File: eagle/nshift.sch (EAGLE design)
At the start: 15 parts, among them IC1 TINY13V-10PU, IC2 7805T, Q1 IRF510, Q2 IRF510

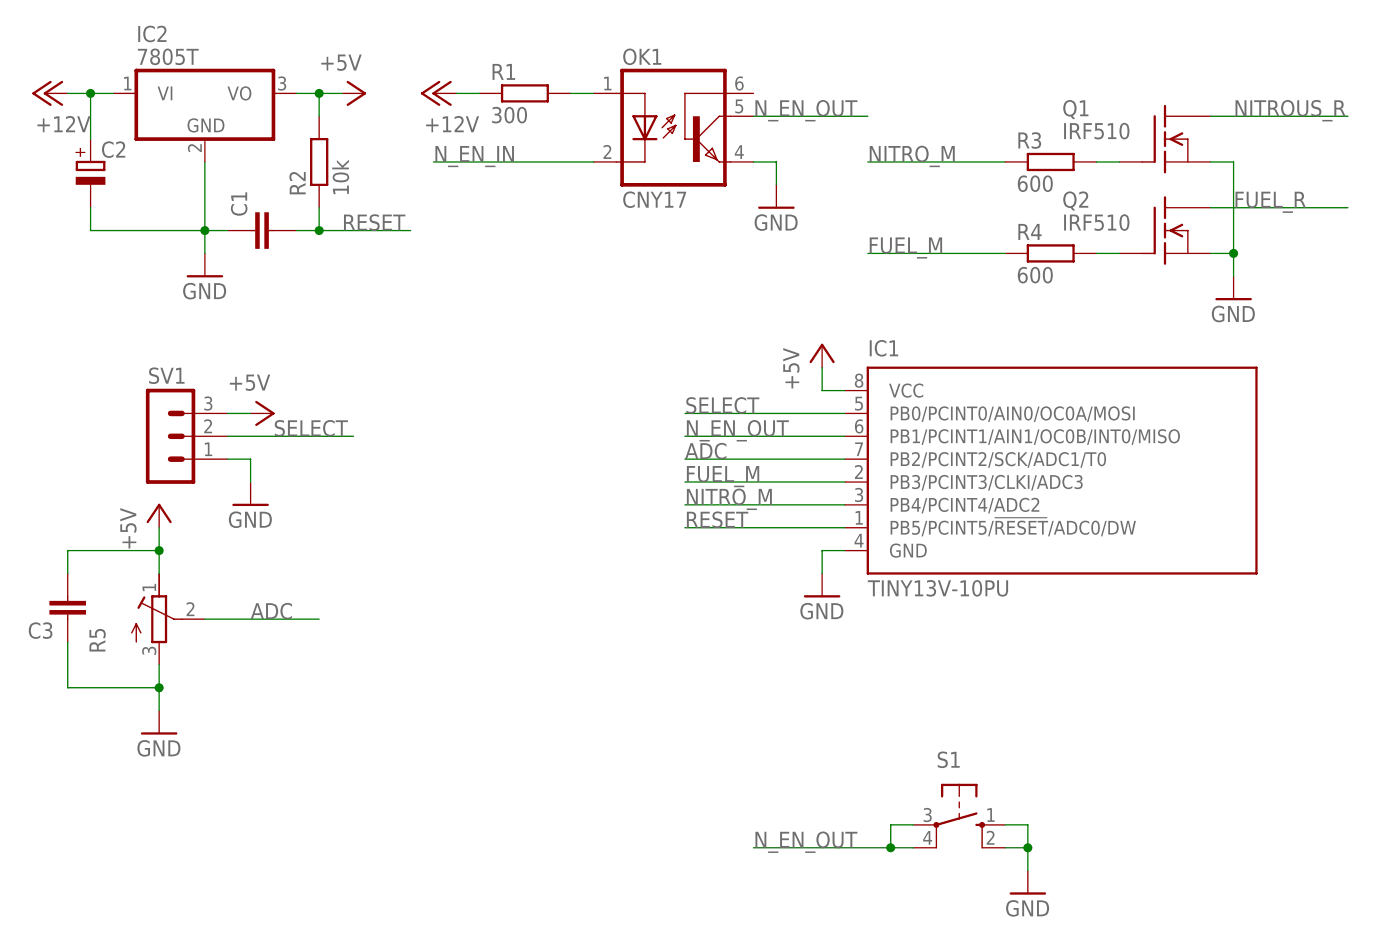
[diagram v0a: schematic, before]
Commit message: refactor for new soic components
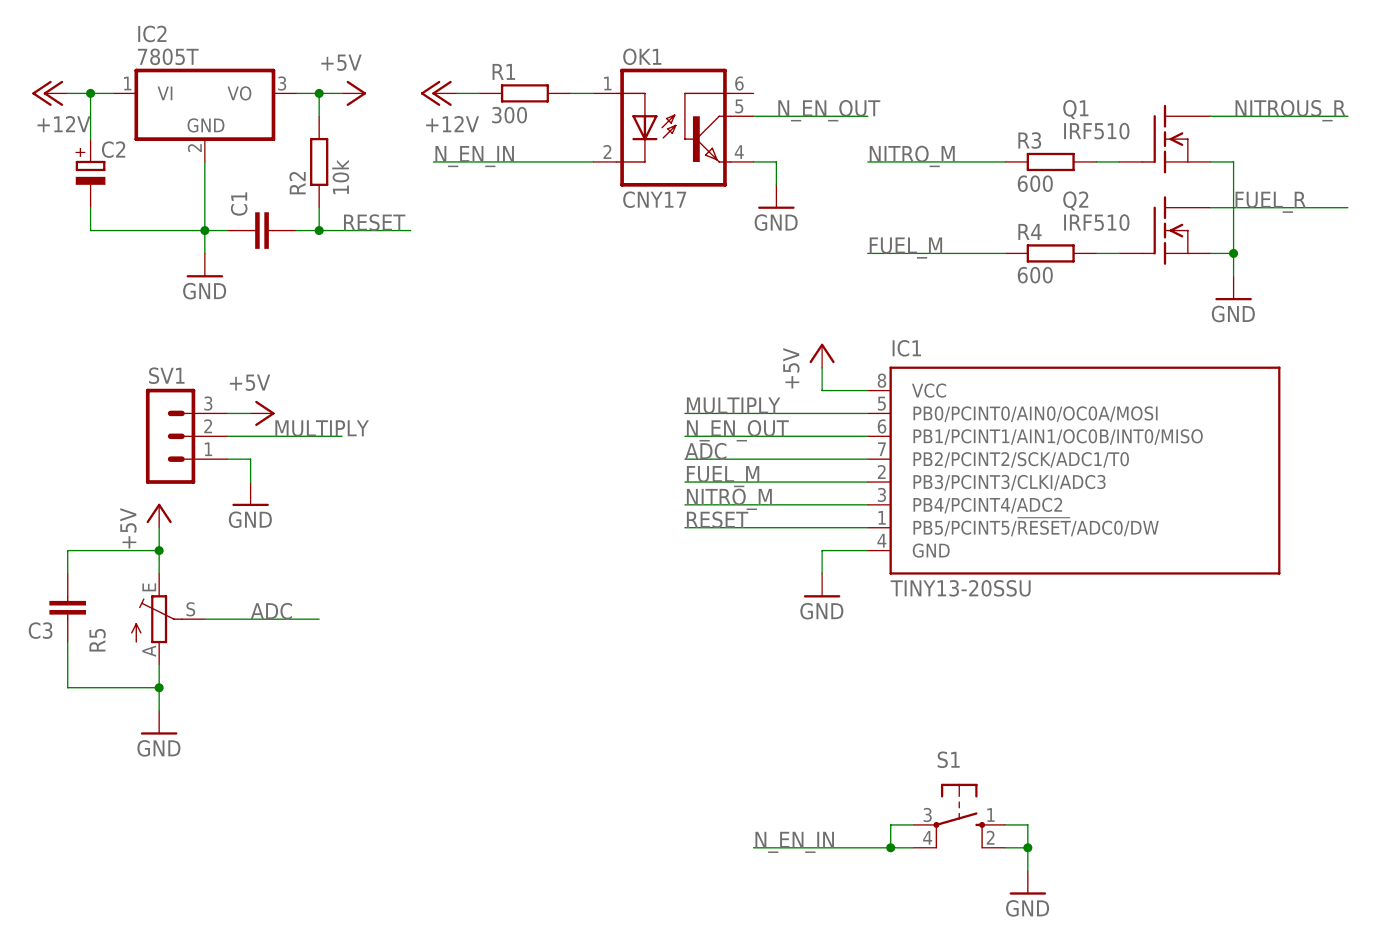
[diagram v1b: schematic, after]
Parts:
- IC1: value TINY13V-10PU -> TINY13-20SSU; device atmel:TINY13V-10PU -> atmel:TINY13-20SSU
- R5: device resistor:R-TRIMMT93XB -> pot:TRIM_EU-CA9V
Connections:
- net SELECT renamed MULTIPLY
- net +5V: now also R5.E; no longer R5.A
- net GND: now also R5.A; no longer R5.E
- net N_EN_IN: now also S1.P, S1.P1
- net N_EN_OUT: no longer S1.P, S1.P1
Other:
- moved on the sheet: IC1
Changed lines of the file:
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@@
 <setting verticaltext="up"/>
 </settings>
-<grid distance="0.05" unitdist="inch" unit="inch" style="dots" multiple="1" display="yes" altdistance="0.01" altunitdist="inch" altunit="inch"/>
+<grid distance="0.1" unitdist="inch" unit="inch" style="lines" multiple="1" display="no" altdistance="0.01" altunitdist="inch" altunit="inch"/>
 <layers>
 <layer number="1" name="Top" color="4" fill="1" visible="no" active="no"/>
@@
 </classes>
 <parts>
-<part name="IC1" library="atmel" deviceset="TINY13" device="PU" technology="V-10"/>
+<part name="IC1" library="atmel" library_urn="urn:adsk.eagle:library:105" deviceset="TINY13" device="SSU" technology="-20" value="TINY13-20SSU"/>
 <part name="OK1" library="optocoupler" deviceset="CNY17" device=""/>
 <part name="Q1" library="transistor-fet" deviceset="IRF510" device=""/>
@@
 <part name="R3" library="resistor" deviceset="R-EU_" device="0207/7" value="600"/>
 <part name="R4" library="resistor" deviceset="R-EU_" device="0207/7" value="600"/>
-<part name="R5" library="resistor" deviceset="R-TRIMM" device="T93XB"/>
+<part name="R5" library="pot" library_urn="urn:adsk.eagle:library:331" deviceset="TRIM_EU-" device="CA9V"/>
 <part name="P+6" library="supply1" deviceset="+5V" device=""/>
 <part name="GND6" library="supply1" deviceset="GND" device=""/>
@@
 </plain>
 <instances>
-<instance part="IC1" gate="G$1" x="106.68" y="43.18"/>
+<instance part="IC1" gate="G$1" x="109.22" y="43.18"/>
 <instance part="OK1" gate="G$1" x="68.58" y="86.36"/>
 <instance part="Q1" gate="G$1" x="121.92" y="83.82"/>
@@
 <instance part="R3" gate="G$1" x="109.22" y="81.28"/>
 <instance part="R4" gate="G$1" x="109.22" y="71.12"/>
-<instance part="R5" gate="G$1" x="10.16" y="30.48"/>
+<instance part="R5" gate="1" x="10.16" y="30.48"/>
 <instance part="P+6" gate="1" x="10.16" y="43.18"/>
 <instance part="GND6" gate="1" x="10.16" y="17.78"/>
@@
 <pinref part="IC1" gate="G$1" pin="GND"/>
 <pinref part="GND2" gate="1" pin="GND"/>
-<wire x1="86.36" y1="38.1" x2="83.82" y2="38.1" width="0.1524" layer="91"/>
+<wire x1="88.9" y1="38.1" x2="83.82" y2="38.1" width="0.1524" layer="91"/>
 <wire x1="83.82" y1="38.1" x2="83.82" y2="35.56" width="0.1524" layer="91"/>
 </segment>
@@
 <segment>
 <pinref part="GND6" gate="1" pin="GND"/>
-<pinref part="R5" gate="G$1" pin="E"/>
+<pinref part="R5" gate="1" pin="A"/>
 <wire x1="10.16" y1="20.32" x2="10.16" y2="22.86" width="0.1524" layer="91"/>
 <pinref part="C3" gate="G$1" pin="1"/>
@@
 <pinref part="IC1" gate="G$1" pin="VCC"/>
 <pinref part="P+3" gate="1" pin="+5V"/>
-<wire x1="86.36" y1="55.88" x2="83.82" y2="55.88" width="0.1524" layer="91"/>
+<wire x1="88.9" y1="55.88" x2="83.82" y2="55.88" width="0.1524" layer="91"/>
 <wire x1="83.82" y1="55.88" x2="83.82" y2="58.42" width="0.1524" layer="91"/>
 </segment>
@@
 </segment>
 <segment>
-<pinref part="R5" gate="G$1" pin="A"/>
+<pinref part="R5" gate="1" pin="E"/>
 <pinref part="P+6" gate="1" pin="+5V"/>
 <wire x1="10.16" y1="35.56" x2="10.16" y2="38.1" width="0.1524" layer="91"/>
@@
 <pinref part="OK1" gate="G$1" pin="COL"/>
 <wire x1="76.2" y1="86.36" x2="88.9" y2="86.36" width="0.1524" layer="91"/>
-<label x="76.2" y="86.36" size="1.778" layer="95"/>
+<label x="78.74" y="86.36" size="1.778" layer="95"/>
 </segment>
 <segment>
 <pinref part="IC1" gate="G$1" pin="PB1/PCINT1/AIN1/OC0B/INT0/MISO"/>
-<wire x1="86.36" y1="50.8" x2="68.58" y2="50.8" width="0.1524" layer="91"/>
+<wire x1="88.9" y1="50.8" x2="68.58" y2="50.8" width="0.1524" layer="91"/>
 <label x="68.58" y="50.8" size="1.778" layer="95"/>
+</segment>
+</net>
+<net name="N_EN_IN" class="0">
+<segment>
+<pinref part="OK1" gate="G$1" pin="C"/>
+<wire x1="58.42" y1="81.28" x2="40.64" y2="81.28" width="0.1524" layer="91"/>
+<label x="40.64" y="81.28" size="1.778" layer="95"/>
 </segment>
 <segment>
@@
 </segment>
 </net>
-<net name="N_EN_IN" class="0">
-<segment>
-<pinref part="OK1" gate="G$1" pin="C"/>
-<wire x1="58.42" y1="81.28" x2="40.64" y2="81.28" width="0.1524" layer="91"/>
-<label x="40.64" y="81.28" size="1.778" layer="95"/>
-</segment>
-</net>
 <net name="FUEL_R" class="0">
 <segment>
@@
 <net name="FUEL_M" class="0">
 <segment>
-<pinref part="IC1" gate="G$1" pin="PB3/PCINT3/CLKI/ADC3"/>
-<wire x1="86.36" y1="45.72" x2="68.58" y2="45.72" width="0.1524" layer="91"/>
-<label x="68.58" y="45.72" size="1.778" layer="95"/>
-</segment>
-<segment>
 <pinref part="R4" gate="G$1" pin="1"/>
 <wire x1="104.14" y1="71.12" x2="88.9" y2="71.12" width="0.1524" layer="91"/>
 <label x="88.9" y="71.12" size="1.778" layer="95"/>
 </segment>
+<segment>
+<pinref part="IC1" gate="G$1" pin="PB3/PCINT3/CLKI/ADC3"/>
+<wire x1="88.9" y1="45.72" x2="68.58" y2="45.72" width="0.1524" layer="91"/>
+<label x="68.58" y="45.72" size="1.778" layer="95"/>
+</segment>
 </net>
 <net name="NITRO_M" class="0">
 <segment>
 <pinref part="IC1" gate="G$1" pin="PB4/PCINT4/ADC2"/>
-<wire x1="86.36" y1="43.18" x2="68.58" y2="43.18" width="0.1524" layer="91"/>
+<wire x1="88.9" y1="43.18" x2="68.58" y2="43.18" width="0.1524" layer="91"/>
 <label x="68.58" y="43.18" size="1.778" layer="95"/>
 </segment>
@@
 <segment>
 <pinref part="IC1" gate="G$1" pin="PB5/PCINT5/!RESET!/ADC0/DW"/>
-<wire x1="86.36" y1="40.64" x2="68.58" y2="40.64" width="0.1524" layer="91"/>
+<wire x1="88.9" y1="40.64" x2="68.58" y2="40.64" width="0.1524" layer="91"/>
 <label x="68.58" y="40.64" size="1.778" layer="95"/>
 </segment>
@@
 <segment>
 <pinref part="IC1" gate="G$1" pin="PB2/PCINT2/SCK/ADC1/T0"/>
-<wire x1="86.36" y1="48.26" x2="68.58" y2="48.26" width="0.1524" layer="91"/>
+<wire x1="88.9" y1="48.26" x2="68.58" y2="48.26" width="0.1524" layer="91"/>
 <label x="68.58" y="48.26" size="1.778" layer="95"/>
 </segment>
 <segment>
-<pinref part="R5" gate="G$1" pin="S"/>
+<pinref part="R5" gate="1" pin="S"/>
 <wire x1="15.24" y1="30.48" x2="27.94" y2="30.48" width="0.1524" layer="91"/>
 <label x="20.32" y="30.48" size="1.778" layer="95"/>
-</segment>
-</net>
-<net name="SELECT" class="0">
-<segment>
-<pinref part="IC1" gate="G$1" pin="PB0/PCINT0/AIN0/OC0A/MOSI"/>
-<wire x1="86.36" y1="53.34" x2="68.58" y2="53.34" width="0.1524" layer="91"/>
-<label x="68.58" y="53.34" size="1.778" layer="95"/>
-</segment>
-<segment>
-<pinref part="SV1" gate="G$1" pin="2"/>
-<wire x1="17.78" y1="50.8" x2="31.75" y2="50.8" width="0.1524" layer="91"/>
-<label x="22.86" y="50.8" size="1.778" layer="95"/>
 </segment>
 </net>
@@
 <pinref part="R3" gate="G$1" pin="2"/>
 <wire x1="116.84" y1="81.28" x2="114.3" y2="81.28" width="0.1524" layer="91"/>
+</segment>
+</net>
+<net name="MULTIPLY" class="0">
+<segment>
+<pinref part="SV1" gate="G$1" pin="2"/>
+<wire x1="17.78" y1="50.8" x2="30.48" y2="50.8" width="0.1524" layer="91"/>
+<label x="22.86" y="50.8" size="1.778" layer="95"/>
+</segment>
+<segment>
+<pinref part="IC1" gate="G$1" pin="PB0/PCINT0/AIN0/OC0A/MOSI"/>
+<wire x1="88.9" y1="53.34" x2="68.58" y2="53.34" width="0.1524" layer="91"/>
+<label x="68.58" y="53.34" size="1.778" layer="95"/>
 </segment>
 </net>
@@
 </schematic>
 </drawing>
+<compatibility>
+<note version="8.2" severity="warning">
+Since Version 8.2, Eagle supports online libraries. The ids
+of those online libraries will not be understood (or retained)
+with this version.
+</note>
+</compatibility>
 </eagle>

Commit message: Готовая плата soic
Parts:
- R2: device resistor:R-EU_0207/10 -> resistor:R-EU_R1206
- R3, R4: device resistor:R-EU_0207/7 -> resistor:R-EU_R1206
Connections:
- net +5V: now also R5.A; no longer R5.E
- net GND: now also R5.E; no longer R5.A
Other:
- moved on the sheet: R3, R4, R5
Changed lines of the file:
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@@
 <layer number="97" name="Info" color="7" fill="1" visible="yes" active="yes"/>
 <layer number="98" name="Guide" color="6" fill="1" visible="yes" active="yes"/>
+<layer number="99" name="SpiceOrder" color="5" fill="1" visible="yes" active="yes"/>
 </layers>
 <schematic xreflabel="%F%N/%S.%C%R" xrefpart="/%S.%C%R">
@@
 <part name="GND3" library="supply1" deviceset="GND" device=""/>
 <part name="GND4" library="supply1" deviceset="GND" device=""/>
-<part name="R2" library="resistor" deviceset="R-EU_" device="0207/10" value="10k"/>
+<part name="R2" library="resistor" library_urn="urn:adsk.eagle:library:348" deviceset="R-EU_" device="R1206" value="10k"/>
 <part name="P+5" library="supply1" deviceset="+5V" device=""/>
 <part name="GND5" library="supply1" deviceset="GND" device=""/>
-<part name="R3" library="resistor" deviceset="R-EU_" device="0207/7" value="600"/>
-<part name="R4" library="resistor" deviceset="R-EU_" device="0207/7" value="600"/>
+<part name="R3" library="resistor" library_urn="urn:adsk.eagle:library:348" deviceset="R-EU_" device="R1206" value="600"/>
+<part name="R4" library="resistor" deviceset="R-EU_" device="R1206" value="600"/>
 <part name="R5" library="pot" library_urn="urn:adsk.eagle:library:331" deviceset="TRIM_EU-" device="CA9V"/>
 <part name="P+6" library="supply1" deviceset="+5V" device=""/>
@@
 <instance part="P+5" gate="1" x="22.86" y="53.34" rot="R270"/>
 <instance part="GND5" gate="1" x="20.32" y="43.18"/>
-<instance part="R3" gate="G$1" x="109.22" y="81.28"/>
-<instance part="R4" gate="G$1" x="109.22" y="71.12"/>
-<instance part="R5" gate="1" x="10.16" y="30.48"/>
+<instance part="R3" gate="G$1" x="106.68" y="81.28"/>
+<instance part="R4" gate="G$1" x="106.68" y="71.12"/>
+<instance part="R5" gate="1" x="10.16" y="30.48" rot="MR180"/>
 <instance part="P+6" gate="1" x="10.16" y="43.18"/>
 <instance part="GND6" gate="1" x="10.16" y="17.78"/>
@@
 <segment>
 <pinref part="GND6" gate="1" pin="GND"/>
-<pinref part="R5" gate="1" pin="A"/>
 <wire x1="10.16" y1="20.32" x2="10.16" y2="22.86" width="0.1524" layer="91"/>
 <pinref part="C3" gate="G$1" pin="1"/>
-<wire x1="10.16" y1="22.86" x2="10.16" y2="25.4" width="0.1524" layer="91"/>
 <wire x1="0" y1="27.94" x2="0" y2="22.86" width="0.1524" layer="91"/>
 <wire x1="0" y1="22.86" x2="10.16" y2="22.86" width="0.1524" layer="91"/>
+<pinref part="R5" gate="1" pin="E"/>
+<wire x1="10.16" y1="25.4" x2="10.16" y2="22.86" width="0.1524" layer="91"/>
 <junction x="10.16" y="22.86"/>
 </segment>
@@
 </segment>
 <segment>
-<pinref part="R5" gate="1" pin="E"/>
 <pinref part="P+6" gate="1" pin="+5V"/>
-<wire x1="10.16" y1="35.56" x2="10.16" y2="38.1" width="0.1524" layer="91"/>
 <pinref part="C3" gate="G$1" pin="2"/>
 <wire x1="10.16" y1="38.1" x2="10.16" y2="40.64" width="0.1524" layer="91"/>
 <wire x1="0" y1="35.56" x2="0" y2="38.1" width="0.1524" layer="91"/>
 <wire x1="0" y1="38.1" x2="10.16" y2="38.1" width="0.1524" layer="91"/>
+<pinref part="R5" gate="1" pin="A"/>
+<wire x1="10.16" y1="35.56" x2="10.16" y2="38.1" width="0.1524" layer="91"/>
 <junction x="10.16" y="38.1"/>
 </segment>
@@
 <segment>
 <pinref part="R4" gate="G$1" pin="1"/>
-<wire x1="104.14" y1="71.12" x2="88.9" y2="71.12" width="0.1524" layer="91"/>
+<wire x1="101.6" y1="71.12" x2="88.9" y2="71.12" width="0.1524" layer="91"/>
 <label x="88.9" y="71.12" size="1.778" layer="95"/>
 </segment>
@@
 <segment>
 <pinref part="R3" gate="G$1" pin="1"/>
-<wire x1="104.14" y1="81.28" x2="88.9" y2="81.28" width="0.1524" layer="91"/>
+<wire x1="101.6" y1="81.28" x2="88.9" y2="81.28" width="0.1524" layer="91"/>
 <label x="88.9" y="81.28" size="1.778" layer="95"/>
 </segment>
@@
 <pinref part="Q2" gate="G$1" pin="G"/>
 <pinref part="R4" gate="G$1" pin="2"/>
-<wire x1="116.84" y1="71.12" x2="114.3" y2="71.12" width="0.1524" layer="91"/>
+<wire x1="116.84" y1="71.12" x2="111.76" y2="71.12" width="0.1524" layer="91"/>
 </segment>
 </net>
@@
 <pinref part="Q1" gate="G$1" pin="G"/>
 <pinref part="R3" gate="G$1" pin="2"/>
-<wire x1="116.84" y1="81.28" x2="114.3" y2="81.28" width="0.1524" layer="91"/>
-</segment>
-</net>
+<wire x1="116.84" y1="81.28" x2="111.76" y2="81.28" width="0.1524" layer="91"/>
+</segment>
+</net>
